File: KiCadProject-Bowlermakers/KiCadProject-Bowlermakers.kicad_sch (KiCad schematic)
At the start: 3 parts, among them U1 STM32F091C_B-C_Tx, U2 AK9753, U3 24LC32

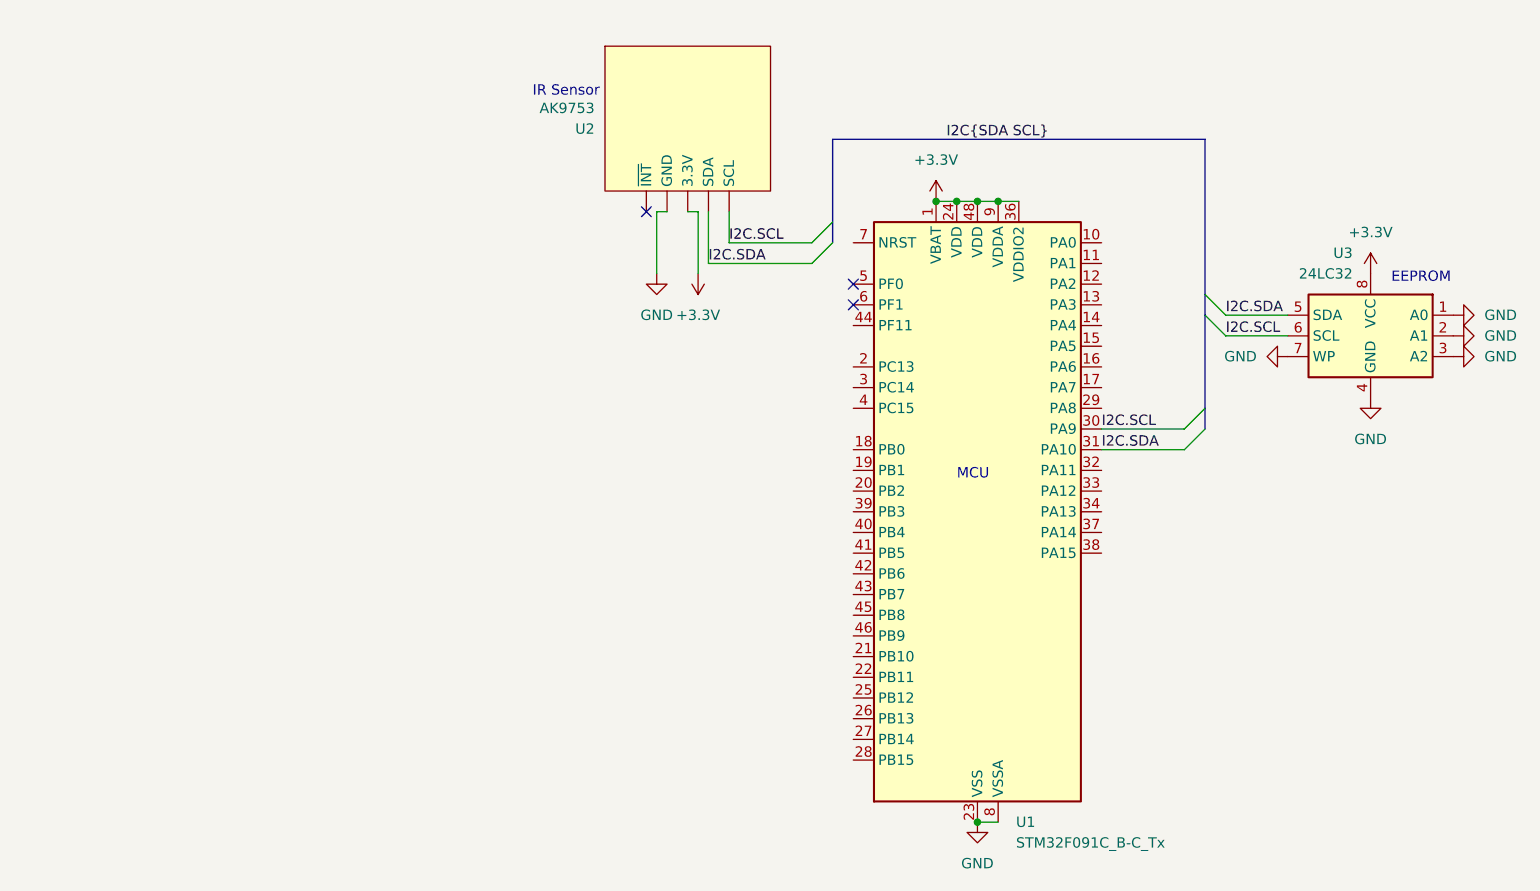
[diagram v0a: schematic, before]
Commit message: eeprom, display added to schematic
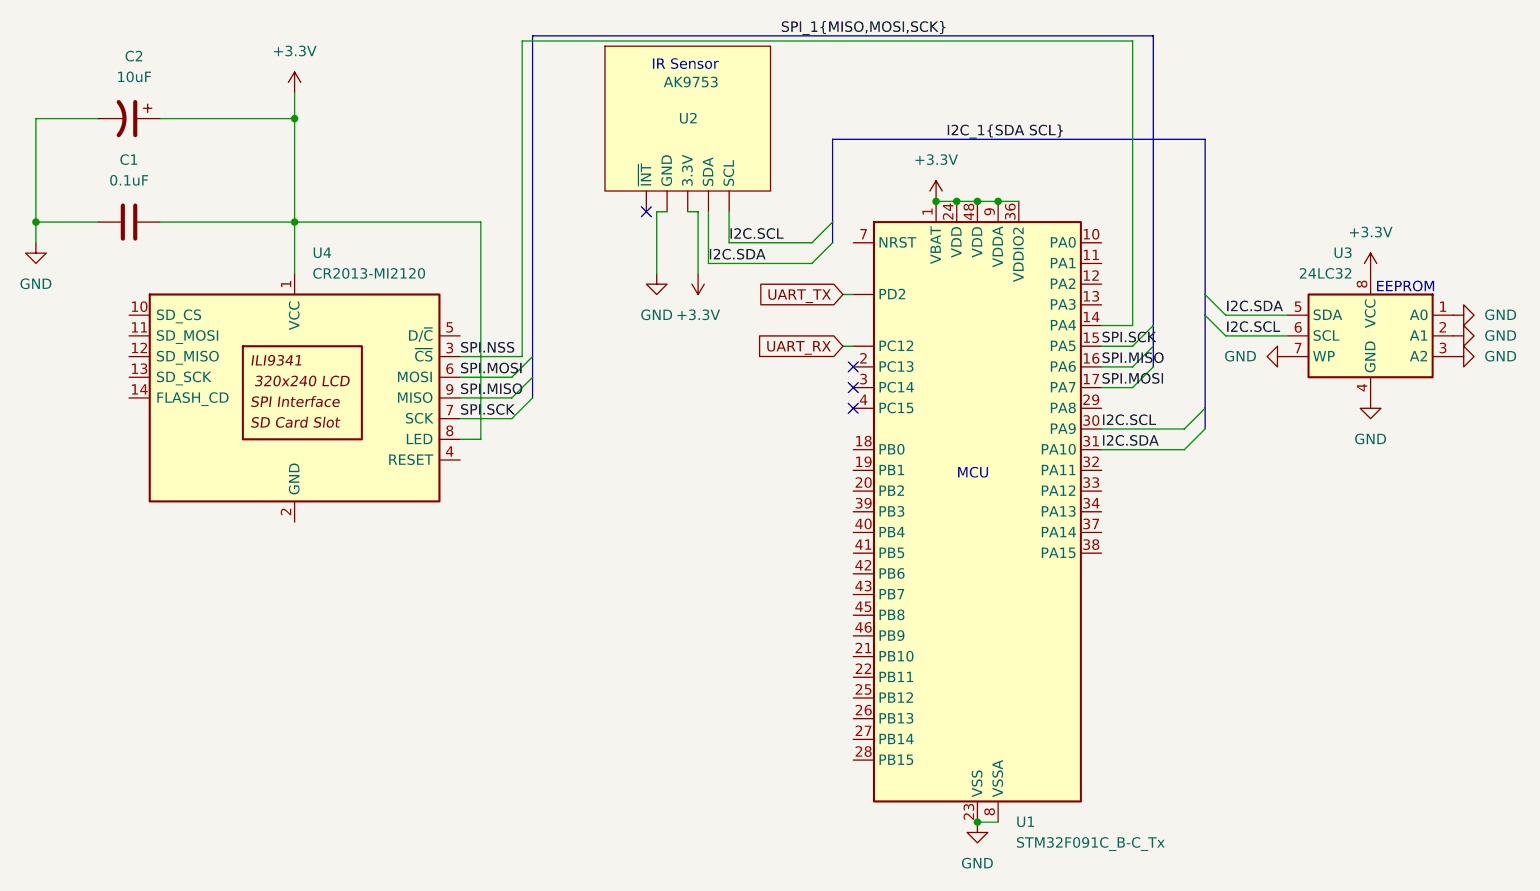
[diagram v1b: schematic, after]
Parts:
- removed U1: STM32F091C_B-C_Tx, Package_QFP:LQFP-48_7x7mm_P0.5mm, symbol stm32f091c_b-c_tx:STM32F091C_B-C_Tx
- added C1: 0.1uF, symbol Device:C
- added C2: 10uF, symbol Device:C_Polarized_US
- added U1: STM32F091C_B-C_Tx, Package_QFP:LQFP-48_7x7mm_P0.5mm, symbol MCU_ST_STM32F0:STM32F091C_B-C_Tx
- added U4: CR2013-MI2120, Display:CR2013-MI2120, symbol Driver_Display:CR2013-MI2120
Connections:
- net +3.3V: now also C1.2, C2.1, U1.1 (VBAT), U1.24 (VDD), U1.36 (VDDIO2), U1.48 (VDD), U1.9 (VDDA), U4.1 (VCC), U4.8 (LED)
- net GND: now also C1.1, C2.2, U1.23 (VSS), U1.35 (VSS), U1.47 (VSS), U1.8 (VSSA)
- net I2C.SCL: now also U1.30 (PA9)
- net I2C.SDA: now also U1.31 (PA10)
- new net SPI.MISO: U1.16 (PA6), U4.9 (MISO)
- new net SPI.MOSI: U1.17 (PA7), U4.6 (MOSI)
- new net SPI.NSS: U1.14 (PA4), U4.3 (~{CS})
- new net SPI.SCK: U1.15 (PA5), U4.7 (SCK)
- new net UART_RX: U1. (PD2)
- new net UART_TX: U1. (PD2)
- no-connect marks 3 -> 4

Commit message: Add EEPROM, utility, TTY, and IR driver headers and implementations
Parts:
- added SW1, SW2: SW_MEC_5E, symbol Switch:SW_MEC_5E
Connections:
- net GND: now also SW1.1
- net at U1.18 (PB0): now also SW1.4 (A)
- net at U1.39 (PB3): now also SW2.4 (A)
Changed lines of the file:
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@@
+    (stroke (width 0) (type default))
+  )
+  (wire (pts (xy 103.505 67.31) (xy 103.505 72.39))
     (stroke (width 0) (type default))
   )
@@
     (stroke (width 0) (type default))
   )
+  (wire (pts (xy 99.06 72.39) (xy 103.505 72.39))
+    (stroke (width 0) (type default))
+  )
   (wire (pts (xy 22.86 39.37) (xy 30.48 39.37))
     (stroke (width 0) (type default))
@@
     (stroke (width 0) (type default))
   )
+  (wire (pts (xy 106.68 85.09) (xy 106.68 74.93))
+    (stroke (width 0) (type default))
+  )
   (wire (pts (xy 157.48 17.145) (xy 82.55 17.145))
     (stroke (width 0) (type default))
@@
     (stroke (width 0) (type default))
   )
+  (wire (pts (xy 123.19 67.31) (xy 103.505 67.31))
+    (stroke (width 0) (type default))
+  )
   (wire (pts (xy 118.11 44.45) (xy 105.41 44.45))
     (stroke (width 0) (type default))
@@
     (stroke (width 0) (type default))
   )
+  (wire (pts (xy 85.09 72.39) (xy 88.9 72.39))
+    (stroke (width 0) (type default))
+  )
   (wire (pts (xy 107.95 38.1) (xy 107.95 41.91))
     (stroke (width 0) (type default))
@@
     (stroke (width 0) (type default))
   )
+  (wire (pts (xy 99.06 85.09) (xy 106.68 85.09))
+    (stroke (width 0) (type default))
+  )
   (wire (pts (xy 138.43 36.83) (xy 140.97 36.83))
     (stroke (width 0) (type default))
   )
+  (wire (pts (xy 106.68 74.93) (xy 123.19 74.93))
+    (stroke (width 0) (type default))
+  )
   (wire (pts (xy 153.67 57.15) (xy 157.48 57.15))
     (stroke (width 0) (type default))
@@
     (effects (font (size 1.27 1.27)) (justify left bottom))
   )
-  (label "SPI.SCK" (at 74.93 63.5 0)
-    (effects (font (size 1.27 1.27)) (justify left bottom))
-  )
-  (label "SPI.MISO" (at 153.67 57.15 0)
+  (label "SPI.SCK" (at 74.93 63.5 0) (fields_autoplaced)
+    (effects (font (size 1.27 1.27)) (justify left bottom))
+  )
+  (label "SPI.MISO" (at 153.67 57.15 0) (fields_autoplaced)
     (effects (font (size 1.27 1.27)) (justify left bottom))
   )
@@
     (effects (font (size 1.27 1.27)) (justify left bottom))
   )
-  (label "SPI.MISO" (at 74.93 60.96 0)
+  (label "SPI.MISO" (at 74.93 60.96 0) (fields_autoplaced)
     (effects (font (size 1.27 1.27)) (justify left bottom))
   )
@@
     (effects (font (size 1.27 1.27)) (justify left bottom))
   )
-  (label "SPI.SCK" (at 153.67 54.61 0)
-    (effects (font (size 1.27 1.27)) (justify left bottom))
-  )
-  (label "SPI.MOSI" (at 153.67 59.69 0)
+  (label "SPI.SCK" (at 153.67 54.61 0) (fields_autoplaced)
+    (effects (font (size 1.27 1.27)) (justify left bottom))
+  )
+  (label "SPI.MOSI" (at 153.67 59.69 0) (fields_autoplaced)
     (effects (font (size 1.27 1.27)) (justify left bottom))
   )
@@
     (effects (font (size 1.27 1.27)) (justify left bottom))
   )
-  (label "SPI.MOSI" (at 74.93 58.42 0)
+  (label "SPI.MOSI" (at 74.93 58.42 0) (fields_autoplaced)
     (effects (font (size 1.27 1.27)) (justify left bottom))
   )
@@
     )
   )
+  (symbol (lib_id "Switch:SW_MEC_5E") (at 93.98 87.63 0) (unit 1)
+    (in_bom yes) (on_board yes) (dnp no) (fields_autoplaced)
+    (property "Reference" "SW2" (at 93.98 77.47 0)
+      (effects (font (size 1.27 1.27)))
+    )
+    (property "Value" "SW_MEC_5E" (at 93.98 80.01 0)
+      (effects (font (size 1.27 1.27)))
+    )
+    (property "Footprint" "" (at 93.98 80.01 0)
+      (effects (font (size 1.27 1.27)) hide)
+    )
+    (property "Datasheet" "http://www.apem.com/int/index.php?controller=attachment&id_attachment=1371" (at 93.98 80.01 0)
+      (effects (font (size 1.27 1.27)) hide)
+    )
+    (pin "4")
+    (pin "3")
+    (pin "2")
+    (pin "1")
+    (instances
+      (project "KiCadProject-Bowlermakers"
+        (path "/e74fae95-e8dd-4ef2-885c-f603f5e13291"
+          (reference "SW2") (unit 1)
+        )
+      )
+    )
+  )
   (symbol (lib_id "power:GND") (at 22.86 41.91 0) (unit 1)
     (in_bom yes) (on_board yes) (dnp no) (fields_autoplaced)
@@
         (path "/e74fae95-e8dd-4ef2-885c-f603f5e13291"
           (reference "#PWR03") (unit 1)
+        )
+      )
+    )
+  )
+  (symbol (lib_id "power:GND") (at 85.09 72.39 270) (unit 1)
+    (in_bom yes) (on_board yes) (dnp no) (fields_autoplaced)
+    (property "Reference" "#PWR013" (at 78.74 72.39 0)
+      (effects (font (size 1.27 1.27)) hide)
+    )
+    (property "Value" "GND" (at 81.915 72.39 90)
+      (effects (font (size 1.27 1.27)) (justify right))
+    )
+    (property "Footprint" "" (at 85.09 72.39 0)
+      (effects (font (size 1.27 1.27)) hide)
+    )
+    (property "Datasheet" "" (at 85.09 72.39 0)
+      (effects (font (size 1.27 1.27)) hide)
+    )
+    (pin "1")
+    (instances
+      (project "KiCadProject-Bowlermakers"
+        (path "/e74fae95-e8dd-4ef2-885c-f603f5e13291"
+          (reference "#PWR013") (unit 1)
         )
       )
@@
         )
       )
+    )
+  )
+  (symbol (lib_id "Switch:SW_MEC_5E") (at 93.98 74.93 0) (unit 1)
+    (in_bom yes) (on_board yes) (dnp no) (fields_autoplaced)
+    (property "Reference" "SW1" (at 93.98 64.77 0)
+      (effects (font (size 1.27 1.27)))
+    )
+    (property "Value" "SW_MEC_5E" (at 93.98 67.31 0)
+      (effects (font (size 1.27 1.27)))
+    )
+    (property "Footprint" "" (at 93.98 67.31 0)
+      (effects (font (size 1.27 1.27)) hide)
+    )
+    (property "Datasheet" "http://www.apem.com/int/index.php?controller=attachment&id_attachment=1371" (at 93.98 67.31 0)
+      (effects (font (size 1.27 1.27)) hide)
+    )
+    (pin "4")
+    (pin "3")
+    (pin "2")
+    (pin "1")
+    (instances
+      (project "KiCadProject-Bowlermakers"
+        (path "/e74fae95-e8dd-4ef2-885c-f603f5e13291"
+          (reference "SW1") (unit 1)
+        )
+      )

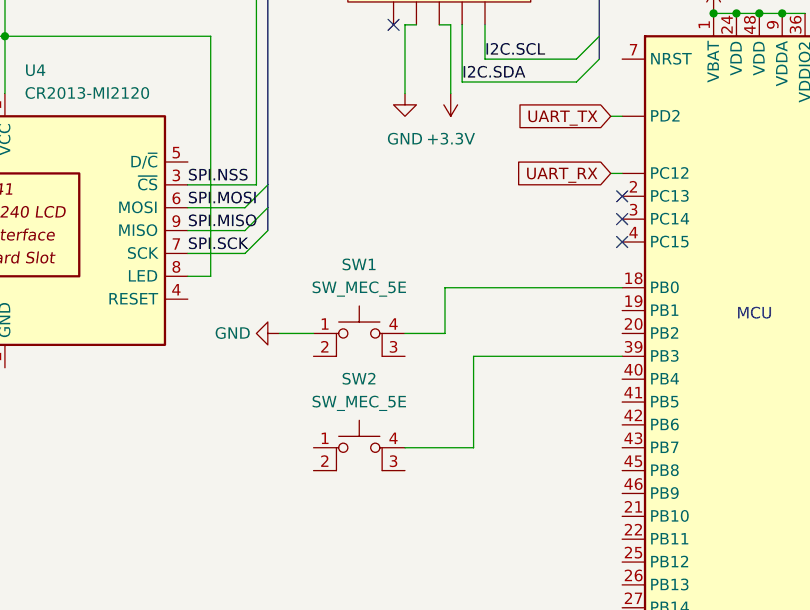
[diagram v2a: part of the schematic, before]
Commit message: add DC/Reset pins to schematic
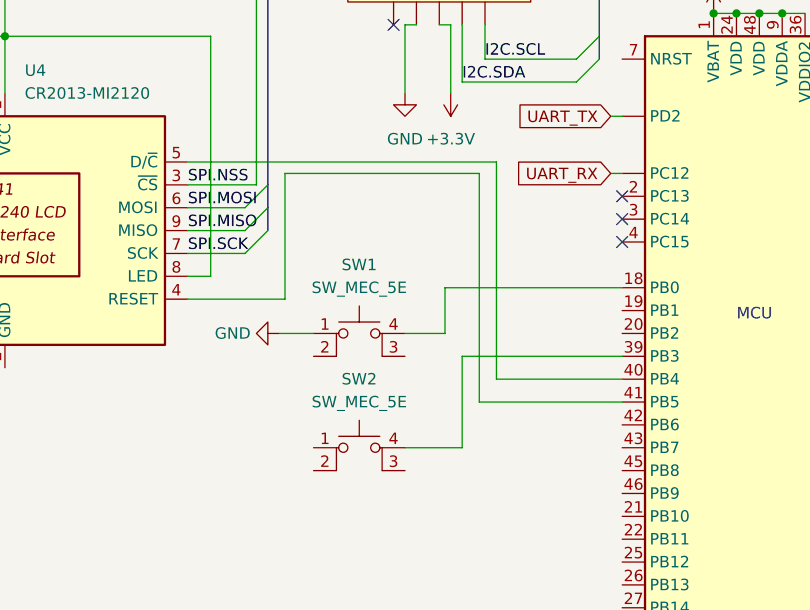
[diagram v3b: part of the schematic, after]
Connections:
- net at U4.4 (RESET): now also U1.41 (PB5)
- net at U4.5 (D/~{C}): now also U1.40 (PB4)
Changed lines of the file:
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@@
+    (stroke (width 0) (type default))
+  )
+  (wire (pts (xy 107.315 54.61) (xy 107.315 80.01))
     (stroke (width 0) (type default))
   )
@@
     (stroke (width 0) (type default))
   )
-  (wire (pts (xy 106.68 85.09) (xy 106.68 74.93))
+  (wire (pts (xy 105.41 85.09) (xy 105.41 74.93))
+    (stroke (width 0) (type default))
+  )
+  (wire (pts (xy 85.725 68.58) (xy 85.725 54.61))
     (stroke (width 0) (type default))
   )
@@
     (stroke (width 0) (type default))
   )
+  (wire (pts (xy 74.93 68.58) (xy 85.725 68.58))
+    (stroke (width 0) (type default))
+  )
   (wire (pts (xy 77.47 66.04) (xy 77.47 39.37))
     (stroke (width 0) (type default))
@@
   )
   (wire (pts (xy 135.89 36.83) (xy 138.43 36.83))
+    (stroke (width 0) (type default))
+  )
+  (wire (pts (xy 74.93 53.34) (xy 109.22 53.34))
     (stroke (width 0) (type default))
   )
@@
     (stroke (width 0) (type default))
   )
+  (wire (pts (xy 109.22 53.34) (xy 109.22 77.47))
+    (stroke (width 0) (type default))
+  )
   (wire (pts (xy 38.1 26.67) (xy 54.61 26.67))
     (stroke (width 0) (type default))
@@
     (stroke (width 0) (type default))
   )
-  (wire (pts (xy 99.06 85.09) (xy 106.68 85.09))
+  (wire (pts (xy 99.06 85.09) (xy 105.41 85.09))
     (stroke (width 0) (type default))
   )
@@
     (stroke (width 0) (type default))
   )
-  (wire (pts (xy 106.68 74.93) (xy 123.19 74.93))
+  (wire (pts (xy 105.41 74.93) (xy 123.19 74.93))
     (stroke (width 0) (type default))
   )
@@
     (stroke (width 0) (type default))
   )
+  (wire (pts (xy 109.22 77.47) (xy 123.19 77.47))
+    (stroke (width 0) (type default))
+  )
+  (wire (pts (xy 85.725 54.61) (xy 107.315 54.61))
+    (stroke (width 0) (type default))
+  )
   (wire (pts (xy 138.43 113.03) (xy 140.97 113.03))
     (stroke (width 0) (type default))
   )
+  (wire (pts (xy 107.315 80.01) (xy 123.19 80.01))
+    (stroke (width 0) (type default))
+  )

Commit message: update NSS pinout
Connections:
- net LCD.DC: now reaches U1.41 (PB5)
- net LCD.DC: now also U4.5 (D/~{C}); no longer U4.4 (RESET)
- net LCD.RESET: now reaches U1.40 (PB4)
- net LCD.RESET: now also U4.4 (RESET); no longer U4.5 (D/~{C})
- net SPI.NSS renamed SPI.LCD.CS
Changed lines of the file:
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@@
-    (stroke (width 0) (type default))
-  )
-  (wire (pts (xy 107.315 54.61) (xy 107.315 80.01))
     (stroke (width 0) (type default))
   )
@@
     (stroke (width 0) (type default))
   )
+  (wire (pts (xy 109.855 53.34) (xy 109.855 80.01))
+    (stroke (width 0) (type default))
+  )
   (bus (pts (xy 166.37 29.21) (xy 120.65 29.21))
     (stroke (width 0) (type default))
@@
     (stroke (width 0) (type default))
   )
-  (wire (pts (xy 85.725 68.58) (xy 85.725 54.61))
-    (stroke (width 0) (type default))
-  )
   (wire (pts (xy 157.48 17.145) (xy 82.55 17.145))
     (stroke (width 0) (type default))
@@
     (stroke (width 0) (type default))
   )
+  (wire (pts (xy 74.93 53.34) (xy 109.855 53.34))
+    (stroke (width 0) (type default))
+  )
   (bus (pts (xy 160.02 16.51) (xy 160.02 52.07))
     (stroke (width 0) (type default))
@@
     (stroke (width 0) (type default))
   )
+  (wire (pts (xy 74.93 68.58) (xy 107.95 68.58))
+    (stroke (width 0) (type default))
+  )
   (bus (pts (xy 160.02 54.61) (xy 160.02 57.15))
     (stroke (width 0) (type default))
   )
+  (wire (pts (xy 109.855 80.01) (xy 123.19 80.01))
+    (stroke (width 0) (type default))
+  )
   (wire (pts (xy 105.41 38.1) (xy 105.41 44.45))
     (stroke (width 0) (type default))
   )
+  (wire (pts (xy 107.95 77.47) (xy 123.19 77.47))
+    (stroke (width 0) (type default))
+  )
   (wire (pts (xy 153.67 64.77) (xy 163.83 64.77))
     (stroke (width 0) (type default))
@@
     (stroke (width 0) (type default))
   )
+  (wire (pts (xy 107.95 68.58) (xy 107.95 77.47))
+    (stroke (width 0) (type default))
+  )
   (bus (pts (xy 166.37 50.8) (xy 166.37 62.23))
     (stroke (width 0) (type default))
@@
     (stroke (width 0) (type default))
   )
-  (wire (pts (xy 74.93 68.58) (xy 85.725 68.58))
-    (stroke (width 0) (type default))
-  )
   (wire (pts (xy 77.47 66.04) (xy 77.47 39.37))
     (stroke (width 0) (type default))
@@
     (stroke (width 0) (type default))
   )
-  (wire (pts (xy 74.93 53.34) (xy 109.22 53.34))
-    (stroke (width 0) (type default))
-  )
   (wire (pts (xy 85.09 72.39) (xy 88.9 72.39))
     (stroke (width 0) (type default))
@@
     (stroke (width 0) (type default))
   )
-  (wire (pts (xy 109.22 53.34) (xy 109.22 77.47))
-    (stroke (width 0) (type default))
-  )
   (wire (pts (xy 38.1 26.67) (xy 54.61 26.67))
     (stroke (width 0) (type default))
@@
     (stroke (width 0) (type default))
   )
-  (wire (pts (xy 109.22 77.47) (xy 123.19 77.47))
-    (stroke (width 0) (type default))
-  )
-  (wire (pts (xy 85.725 54.61) (xy 107.315 54.61))
-    (stroke (width 0) (type default))
-  )
   (wire (pts (xy 138.43 113.03) (xy 140.97 113.03))
     (stroke (width 0) (type default))
   )
-  (wire (pts (xy 107.315 80.01) (xy 123.19 80.01))
-    (stroke (width 0) (type default))
-  )
   (bus (pts (xy 83.82 55.88) (xy 83.82 58.42))
     (stroke (width 0) (type default))
@@
     (effects (font (size 1.27 1.27)) (justify left bottom))
   )
+  (label "SPI.LCD.CS" (at 153.67 52.07 0) (fields_autoplaced)
+    (effects (font (size 1.27 1.27)) (justify left bottom))
+  )
   (label "I2C.SCL" (at 168.91 53.34 0) (fields_autoplaced)
     (effects (font (size 1.27 1.27)) (justify left bottom))
@@
     (effects (font (size 1.27 1.27)) (justify left bottom))
   )
+  (label "LCD.RESET" (at 113.03 77.47 0) (fields_autoplaced)
+    (effects (font (size 1.27 1.27)) (justify left bottom))
+  )
+  (label "LCD.DC" (at 116.205 80.01 0) (fields_autoplaced)
+    (effects (font (size 1.27 1.27)) (justify left bottom))
+  )
